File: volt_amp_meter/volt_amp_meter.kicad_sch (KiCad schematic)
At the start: 29 parts, among them J1 Molex, J2 ICSP, U2 PIC16F883-IP, U3 LM358, U4 L78L05_SOT89, Y1 4MHz

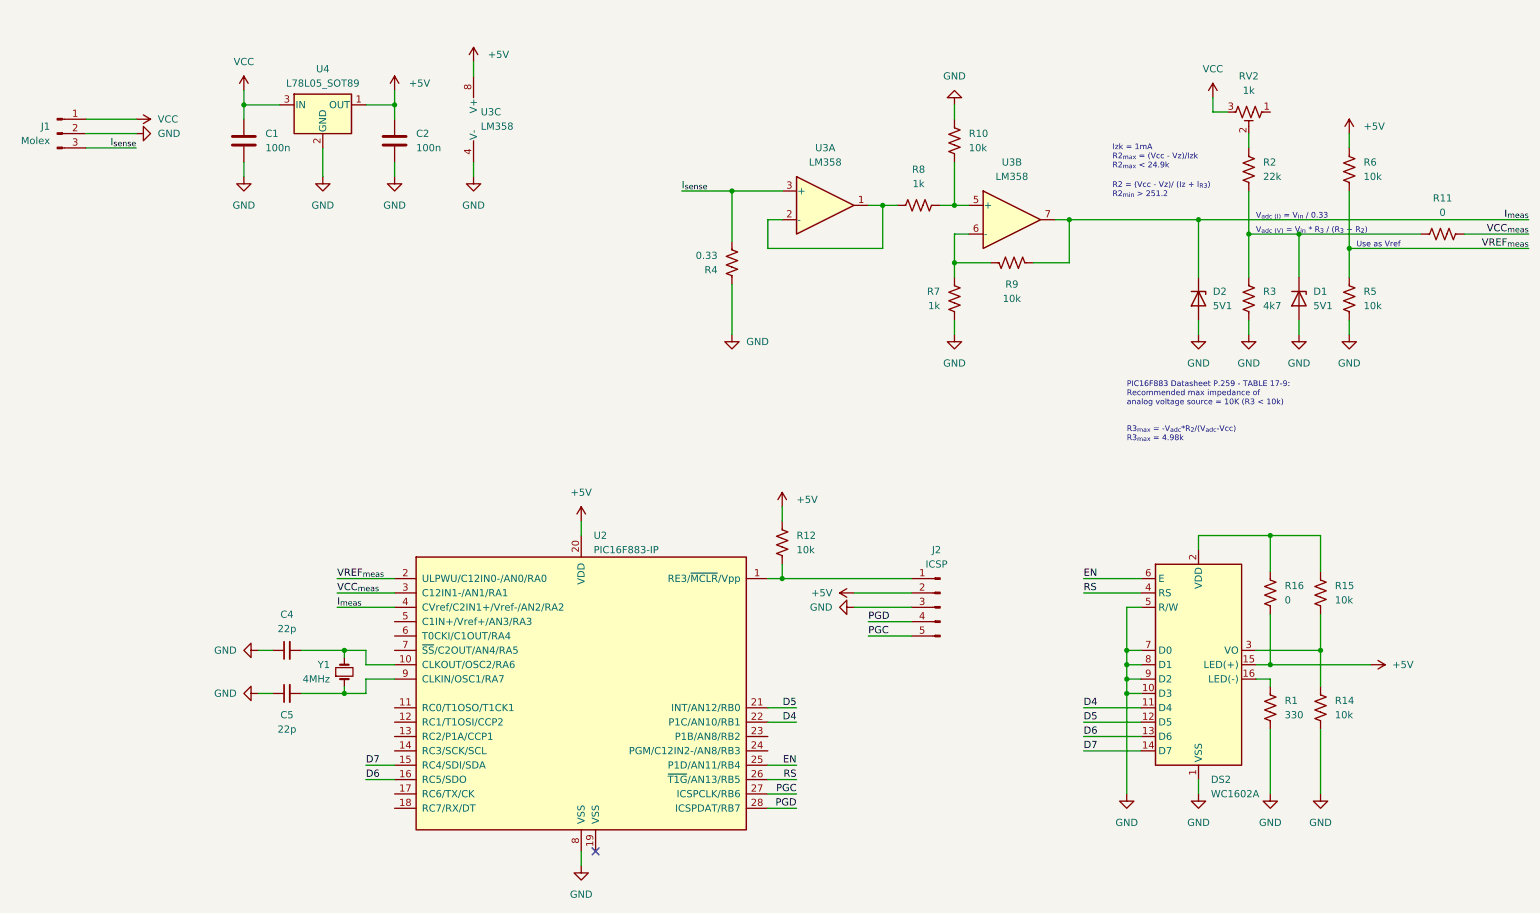
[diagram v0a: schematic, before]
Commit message: [ADD] Panel volt-amp meter from 0-30V and 0-3A (minimal protections)
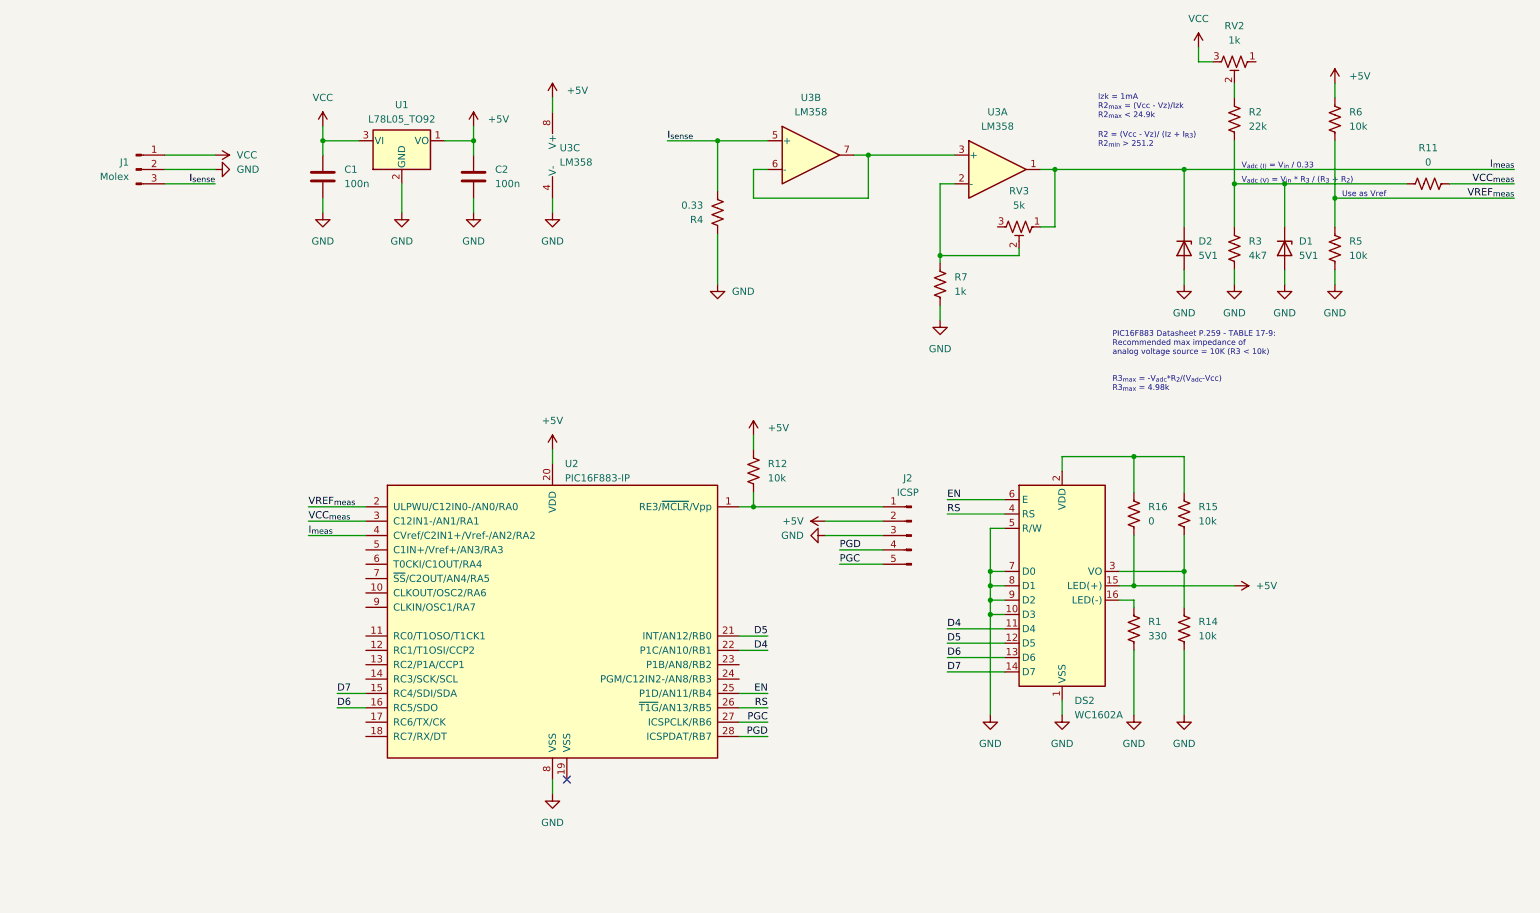
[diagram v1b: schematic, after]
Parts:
- removed C4, C5: 22p, Capacitor_SMD:C_1206_3216Metric_Pad1.33x1.80mm_HandSolder, symbol Device:C_Small
- removed R10, R9: 10k, Resistor_SMD:R_1206_3216Metric_Pad1.30x1.75mm_HandSolder, symbol Device:R_US
- removed R8: 1k, Resistor_SMD:R_1206_3216Metric_Pad1.30x1.75mm_HandSolder, symbol Device:R_US
- removed U4: L78L05_SOT89, Package_TO_SOT_SMD:SOT-89-3, symbol Regulator_Linear:L78L05_SOT89
- removed Y1: 4MHz, Crystal:Crystal_SMD_HC49-SD, symbol Device:Crystal_Small
- added RV3: 5k, Potentiometer_THT:Potentiometer_Bourns_3386C_Horizontal, symbol Device:R_Potentiometer_Trim_US
- added U1: L78L05_TO92, Package_TO_SOT_THT:TO-92_Inline, symbol Regulator_Linear:L78L05_TO92
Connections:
- net +5V: now also U1.1 (VO)
- net GND: now also U1.2 (GND)
- net I_{meas}: now also U3.1, RV3.1; no longer U3.7
- net I_{sense}: now also U3.5 (+); no longer U3.3 (+)
- net VCC: now also U1.3 (VI)
- net at U3.2 (-): now also R7.1, RV3.2; no longer U3.1
- net at U3.6 (-): now also U3.3 (+), U3.7; no longer R7.1
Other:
- moved on the sheet: C1, C2, D1, D2, DS2, J1, J2, R1, R11, R12, R14, R15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
